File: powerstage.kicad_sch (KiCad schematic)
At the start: 29 parts, among them Q1 BSC060N10NS3G, Q2 BSC060N10NS3G, Q3 BSC060N10NS3G, Q4 BSC060N10NS3G, Q5 BSC060N10NS3G, Q6 BSC060N10NS3G, U1 DRV8353SRTAT

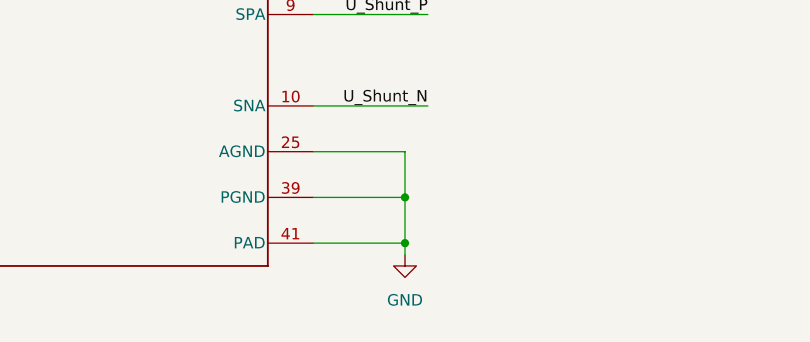
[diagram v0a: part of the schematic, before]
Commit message: edit symbols because of DRC errors (DRV and LM5164)
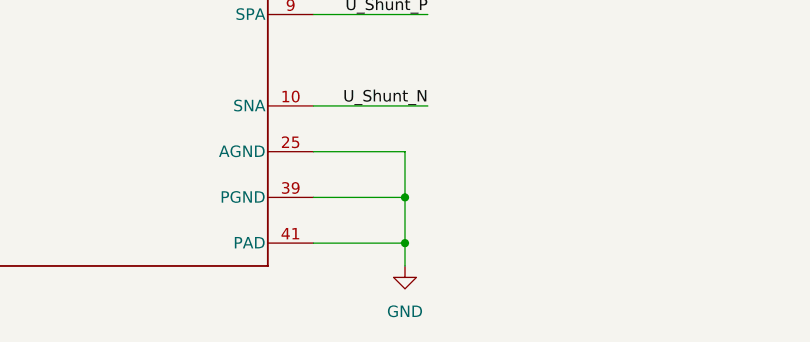
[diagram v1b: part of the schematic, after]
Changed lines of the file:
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@@
 	)
 	(junction
+		(at 142.24 161.29)
+		(diameter 0)
+		(color 0 0 0 0)
+	)
+	(junction
 		(at 52.07 135.89)
 		(diameter 0)
@@
 	)
 	(junction
-		(at 142.24 161.29)
-		(diameter 0)
-		(color 0 0 0 0)
-	)
-	(junction
 		(at 264.16 49.53)
 		(diameter 0)
@@
 	(wire
 		(pts
-			(xy 142.24 161.29) (xy 142.24 162.56)
+			(xy 142.24 161.29) (xy 142.24 163.83)
 		)
 		(stroke
@@
 	(symbol
 		(lib_id "power:GND")
-		(at 142.24 162.56 0)
+		(at 142.24 163.83 0)
 		(unit 1)
 		(body_style 1)
@@
 		(fields_autoplaced yes)
 		(property "Reference" "#PWR09"
-			(at 142.24 168.91 0)
+			(at 142.24 170.18 0)
 			(hide yes)
 			(show_name no)
@@
 		)
 		(property "Value" "GND"
-			(at 142.24 167.64 0)
+			(at 142.24 168.91 0)
 			(show_name no)
 			(do_not_autoplace no)
@@
 		)
 		(property "Footprint" ""
-			(at 142.24 162.56 0)
+			(at 142.24 163.83 0)
 			(hide yes)
 			(show_name no)
@@
 		)
 		(property "Datasheet" ""
-			(at 142.24 162.56 0)
+			(at 142.24 163.83 0)
 			(hide yes)
 			(show_name no)
@@
 		)
 		(property "Description" "Power symbol creates a global label with name \"GND\" , ground"
-			(at 142.24 162.56 0)
+			(at 142.24 163.83 0)
 			(hide yes)
 			(show_name no)

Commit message: update pcb (no errors with XRC)
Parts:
- U1: footprint Custom:DRV8353SRTAT -> MyLib:DRV8353SRTAT
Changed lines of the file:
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@@
 			)
 		)
-		(property "Footprint" "Custom:DRV8353SRTAT"
+		(property "Footprint" "MyLib:DRV8353SRTAT"
 			(at 109.22 97.79 0)
 			(hide yes)
